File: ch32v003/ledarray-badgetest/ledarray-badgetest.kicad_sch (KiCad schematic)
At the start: 84 parts, among them J1 SAO, U1 CH32V003F4U6

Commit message: as ordered
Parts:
- removed R9: 0, Resistor_SMD:R_0402_1005Metric, symbol Device:R
- R1, R2, R3, R4, R5, R6, R7, R8: value 0 -> 22; LCSC C17168 -> C25092
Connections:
- net VCC: now also J1.1 (Pin_1)
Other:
- note added: "LEDs to Try * C965811 Pink, 22 Ohm >> OUT OF STOCK * C5355458 Ice Blue, 22 Ohm * C7371898 Purple, 22 Ohm * C7371900 Red, 47 Ohm * C2977076 Pink, 5mA 22 Ohm * C965807 Blue, 22 Ohm * C965810 Yellow, 22 Ohm * C965804 Emerald, 33 Ohm * C965802 Other Yellow, 49.9 Ohm 22 = C25092 49.9 C25120 33 = C25105"
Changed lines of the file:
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@@
 	(generator_version "9.0")
 	(paper "A4")
+	(text "LEDs to Try\n* C965811 Pink, 22 Ohm >> OUT OF STOCK\n* C5355458 Ice Blue, 22 Ohm\n* C7371898 Purple, 22 Ohm\n* C7371900 Red, 47 Ohm\n* C2977076 Pink, 5mA 22 Ohm\n* C965807 Blue, 22 Ohm\n* C965810 Yellow, 22 Ohm\n\n* C965804 Emerald, 33 Ohm\n* C965802 Other Yellow, 49.9 Ohm\n\n22 = C25092\n49.9 C25120\n33 = C25105"
+		(exclude_from_sim no)
+		(at 207.772 32.004 0)
+		(effects
+			(font
+				(size 1.27 1.27)
+			)
+			(justify left)
+		)
+	)
 	(junction
 		(at 264.16 91.44)
@@
 	(wire
 		(pts
-			(xy 109.22 176.53) (xy 111.76 176.53)
+			(xy 116.84 176.53) (xy 123.19 176.53)
 		)
 		(stroke
@@
 	(wire
 		(pts
-			(xy 119.38 176.53) (xy 123.19 176.53)
-		)
-		(stroke
-			(width 0)
-			(type default)
-		)
-	)
-	(wire
-		(pts
 			(xy 213.36 101.6) (xy 220.98 101.6)
 		)
@@
 			)
 		)
-		(property "Value" "0"
+		(property "Value" "22"
 			(at 204.47 63.5 90)
 			(effects
@@
 			)
 		)
-		(property "LCSC" "C17168"
+		(property "LCSC" "C25092"
 			(at 204.47 63.5 90)
 			(effects
@@
 	)
 	(symbol
-		(lib_id "Device:R")
-		(at 115.57 176.53 90)
-		(unit 1)
-		(exclude_from_sim no)
-		(in_bom yes)
-		(on_board yes)
-		(dnp no)
-		(property "Reference" "R9"
-			(at 115.57 174.498 90)
-			(effects
-				(font
-					(size 1.27 1.27)
-				)
-			)
-		)
-		(property "Value" "0"
-			(at 115.57 176.53 90)
-			(effects
-				(font
-					(size 1.27 1.27)
-				)
-			)
-		)
-		(property "Footprint" "Resistor_SMD:R_0402_1005Metric"
-			(at 115.57 178.308 90)
-			(effects
-				(font
-					(size 1.27 1.27)
-				)
-				(hide yes)
-			)
-		)
-		(property "Datasheet" "~"
-			(at 115.57 176.53 0)
-			(effects
-				(font
-					(size 1.27 1.27)
-				)
-				(hide yes)
-			)
-		)
-		(property "Description" "Resistor"
-			(at 115.57 176.53 0)
-			(effects
-				(font
-					(size 1.27 1.27)
-				)
-				(hide yes)
-			)
-		)
-		(property "LCSC" "C17168"
-			(at 115.57 176.53 90)
-			(effects
-				(font
-					(size 1.27 1.27)
-				)
-				(hide yes)
-			)
-		)
-		(pin "2"
-		)
-		(pin "1"
-		)
-		(instances
-			(project "ledarray-badgetest"
-				(path "/7a961afe-69e2-43ca-af9e-929b11778488"
-					(reference "R9")
-					(unit 1)
-				)
-			)
-		)
-	)
-	(symbol
 		(lib_id "Device:LED_45deg")
 		(at 238.76 104.14 0)
@@
 			)
 		)
-		(property "Value" "0"
+		(property "Value" "22"
 			(at 204.47 71.12 90)
 			(effects
@@
 			)
 		)
-		(property "LCSC" "C17168"
+		(property "LCSC" "C25092"
 			(at 204.47 71.12 90)
 			(effects
@@
 			)
 		)
-		(property "Value" "0"
+		(property "Value" "22"
 			(at 204.47 116.84 90)
 			(effects
@@
 			)
 		)
-		(property "LCSC" "C17168"
+		(property "LCSC" "C25092"
 			(at 204.47 116.84 90)
 			(effects
@@
 			)
 		)
-		(property "Value" "0"
+		(property "Value" "22"
 			(at 204.47 101.6 90)
 			(effects
@@
 			)
 		)
-		(property "LCSC" "C17168"
+		(property "LCSC" "C25092"
 			(at 204.47 101.6 90)
 			(effects
@@
 			)
 		)
-		(property "Value" "0"
+		(property "Value" "22"
 			(at 204.47 93.98 90)
 			(effects
@@
 			)
 		)
-		(property "LCSC" "C17168"
+		(property "LCSC" "C25092"
 			(at 204.47 93.98 90)
 			(effects
@@
 			)
 		)
-		(property "Value" "0"
+		(property "Value" "22"
 			(at 204.47 78.74 90)
 			(effects
@@
 			)
 		)
-		(property "LCSC" "C17168"
+		(property "LCSC" "C25092"
 			(at 204.47 78.74 90)
 			(effects
@@
 			)
 		)
-		(property "Value" "0"
+		(property "Value" "22"
 			(at 204.47 109.22 90)
 			(effects
@@
 			)
 		)
-		(property "LCSC" "C17168"
+		(property "LCSC" "C25092"
 			(at 204.47 109.22 90)
 			(effects
@@
 			)
 		)
-		(property "Value" "0"
+		(property "Value" "22"
 			(at 204.47 86.36 90)
 			(effects
@@
 			)
 		)
-		(property "LCSC" "C17168"
+		(property "LCSC" "C25092"
 			(at 204.47 86.36 90)
 			(effects
@@
 	(symbol
 		(lib_id "power:VCC")
-		(at 109.22 176.53 0)
+		(at 116.84 176.53 0)
 		(unit 1)
 		(exclude_from_sim no)
@@
 		(fields_autoplaced yes)
 		(property "Reference" "#PWR06"
-			(at 109.22 180.34 0)
+			(at 116.84 180.34 0)
 			(effects
 				(font
@@
 		)
 		(property "Value" "VCC"
-			(at 109.22 171.45 0)
+			(at 116.84 171.45 0)
 			(effects
 				(font
@@
 		)
 		(property "Footprint" ""
-			(at 109.22 176.53 0)
+			(at 116.84 176.53 0)
 			(effects
 				(font
@@
 		)
 		(property "Datasheet" ""
-			(at 109.22 176.53 0)
+			(at 116.84 176.53 0)
 			(effects
 				(font
@@
 		)
 		(property "Description" "Power symbol creates a global label with name \"VCC\""
-			(at 109.22 176.53 0)
+			(at 116.84 176.53 0)
 			(effects
 				(font

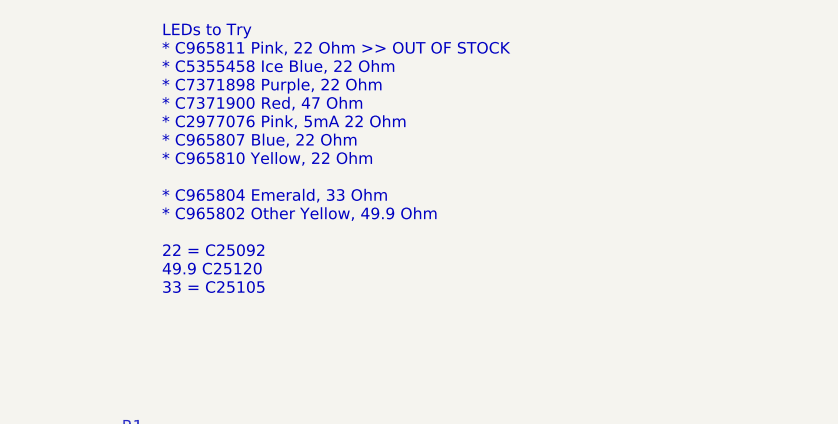
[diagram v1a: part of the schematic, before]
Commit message: Update with notes about which board is which
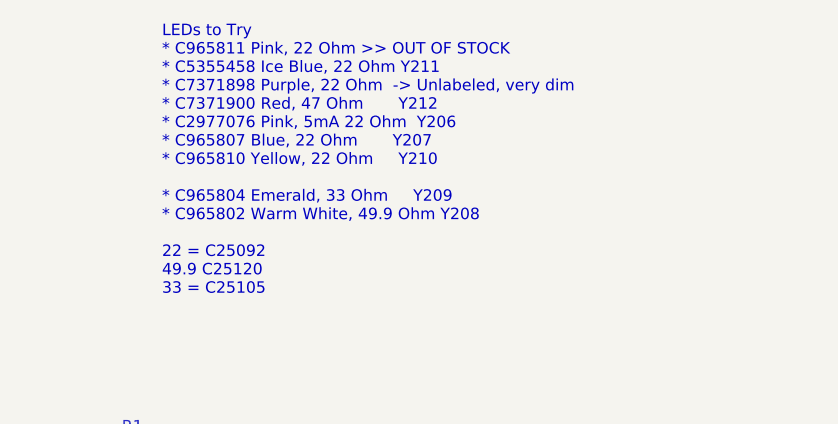
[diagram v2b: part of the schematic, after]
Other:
- note added: "LEDs to Try * C965811 Pink, 22 Ohm >> OUT OF STOCK * C5355458 Ice Blue, 22 Ohm Y211 * C7371898 Purple, 22 Ohm -> Unlabeled, very dim * C7371900 Red, 47 Ohm Y212 * C2977076 Pink, 5mA 22 Ohm Y206 * C965807 Blue, 22 Ohm Y207 * C965810 Yellow, 22 Ohm Y210 * C965804 Emerald, 33 Ohm Y209 * C965802 Warm White, 49.9 Ohm Y208 22 = C25092 49.9 C25120 33 = C25105"
- note removed: "LEDs to Try * C965811 Pink, 22 Ohm >> OUT OF STOCK * C5355458 Ice Blue, 22 Ohm * C7371898 Purple, 22 Ohm * C7371900 Red, 47 Ohm * C2977076 Pink, 5mA 22 Ohm * C965807 Blue, 22 Ohm * C965810 Yellow, 22 Ohm * C965804 Emerald, 33 Ohm * C965802 Other Yellow, 49.9 Ohm 22 = C25092 49.9 C25120 33 = C25105"
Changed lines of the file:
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@@
 	(generator_version "9.0")
 	(paper "A4")
-	(text "LEDs to Try\n* C965811 Pink, 22 Ohm >> OUT OF STOCK\n* C5355458 Ice Blue, 22 Ohm\n* C7371898 Purple, 22 Ohm\n* C7371900 Red, 47 Ohm\n* C2977076 Pink, 5mA 22 Ohm\n* C965807 Blue, 22 Ohm\n* C965810 Yellow, 22 Ohm\n\n* C965804 Emerald, 33 Ohm\n* C965802 Other Yellow, 49.9 Ohm\n\n22 = C25092\n49.9 C25120\n33 = C25105"
+	(text "LEDs to Try\n* C965811 Pink, 22 Ohm >> OUT OF STOCK\n* C5355458 Ice Blue, 22 Ohm Y211\n* C7371898 Purple, 22 Ohm  -> Unlabeled, very dim\n* C7371900 Red, 47 Ohm       Y212\n* C2977076 Pink, 5mA 22 Ohm  Y206\n* C965807 Blue, 22 Ohm       Y207\n* C965810 Yellow, 22 Ohm     Y210\n\n* C965804 Emerald, 33 Ohm     Y209\n* C965802 Warm White, 49.9 Ohm Y208\n\n22 = C25092\n49.9 C25120\n33 = C25105"
 		(exclude_from_sim no)
 		(at 207.772 32.004 0)
